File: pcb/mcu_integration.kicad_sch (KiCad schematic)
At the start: 36 parts, among them J5 DM3BT-DSF-PEJS, M1 MountingHole_Pad, M2 MountingHole_Pad, M3 MountingHole_Pad, M4 MountingHole_Pad, U1 STM32F103RBTx, U6 LM35DM, Y1 ECS-80-18-5PX-GM-TR

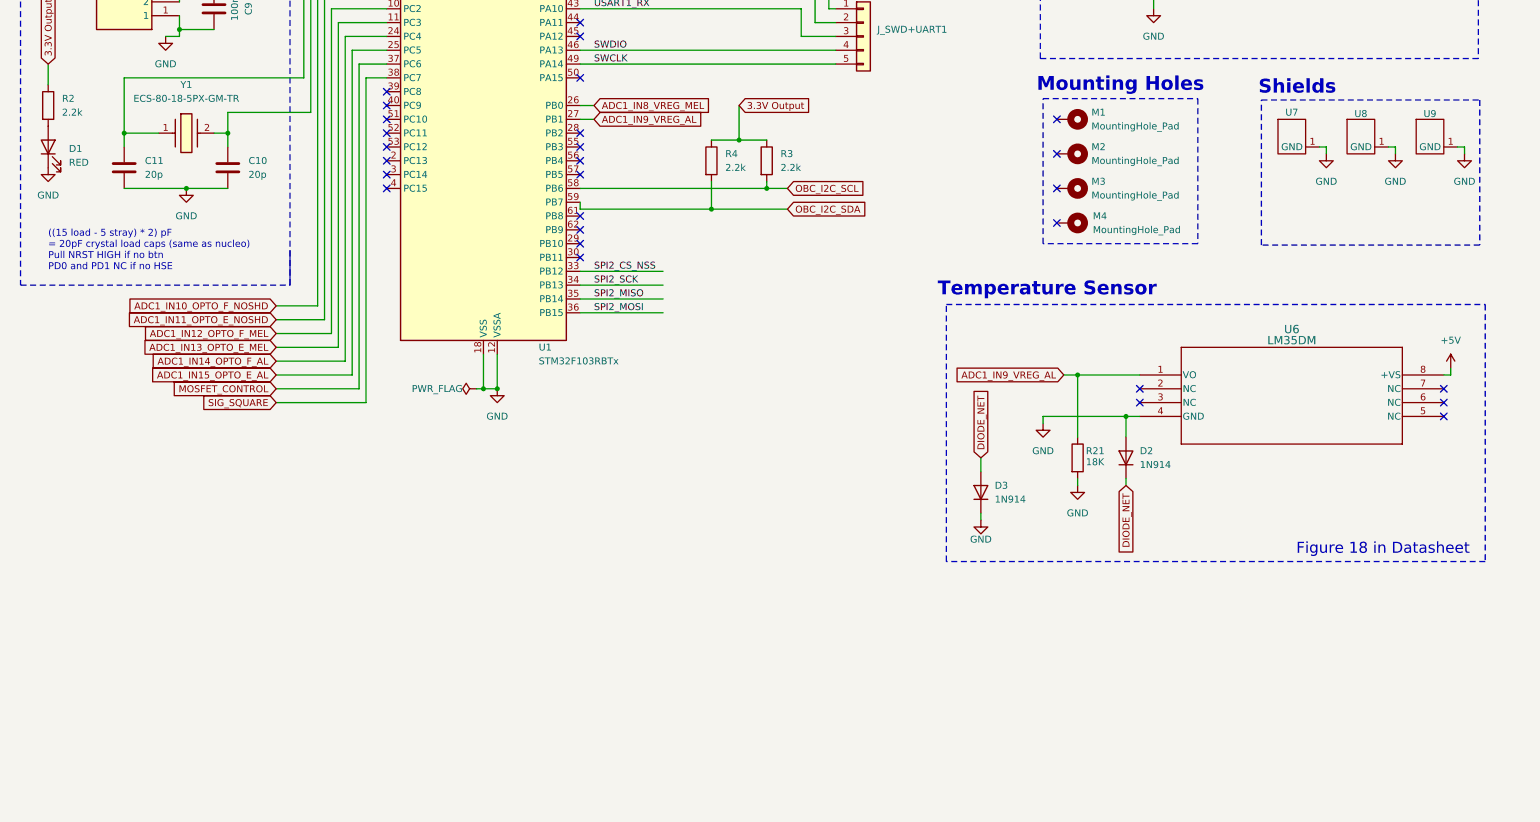
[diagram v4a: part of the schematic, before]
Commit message: Fixed Shield Solder Mask
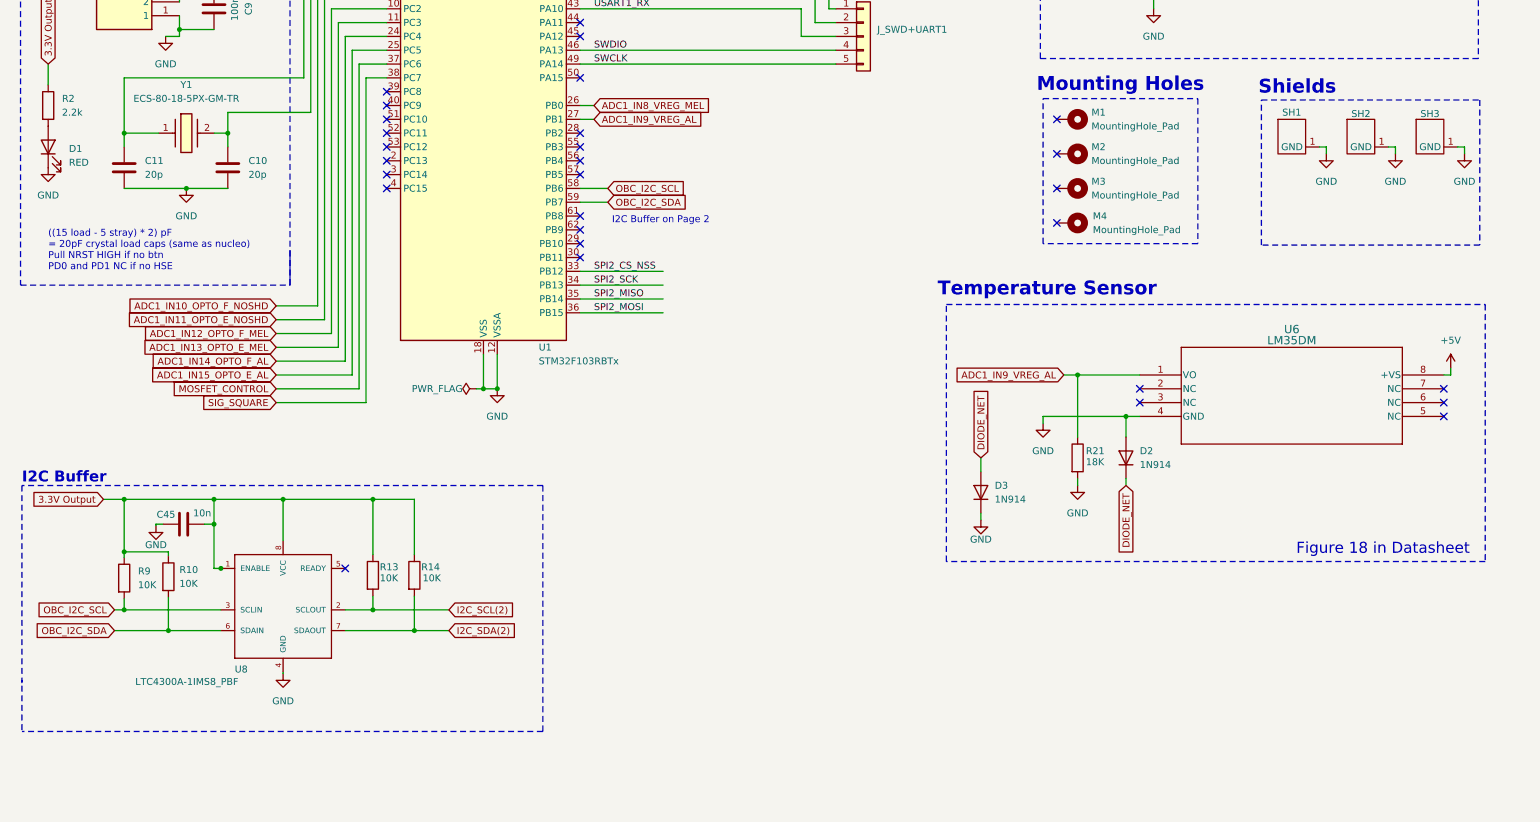
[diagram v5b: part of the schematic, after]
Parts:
- removed R3, R4: 2.2k, Resistor_SMD:R_0402_1005Metric, symbol Device:R
- added C45: 10n, Capacitor_SMD:C_0402_1005Metric, symbol Device:C
- added R10, R13, R14, R9: 10K, Resistor_SMD:R_0402_1005Metric, symbol Device:R
- added U8: LTC4300A-1IMS8_PBF, capstone:LTC4300A-1IMS8_PBF, symbol capstone:LTC4300A-1IMS8_PBF
- renumbered U7 to SH1, U8 to SH2, U9 to SH3
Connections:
- net 3.3V Output: now also C45.2, R10.1, R13.1, R14.1, R9.1, U8.1 (ENABLE), U8.8 (VCC)
- net GND: now also C45.1, U8.4 (GND)
- net OBC_I2C_SCL: now also R9.2, U8.3 (SCLIN)
- net OBC_I2C_SDA: now also R10.2, U8.6 (SDAIN)
- new net I2C_SCL(2): R13.2, U8.2 (SCLOUT)
- new net I2C_SDA(2): R14.2, U8.7 (SDAOUT)
- no-connect marks 34 -> 35
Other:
- note added: "I2C Buffer"
- note added: "I2C Buffer on Page 2"

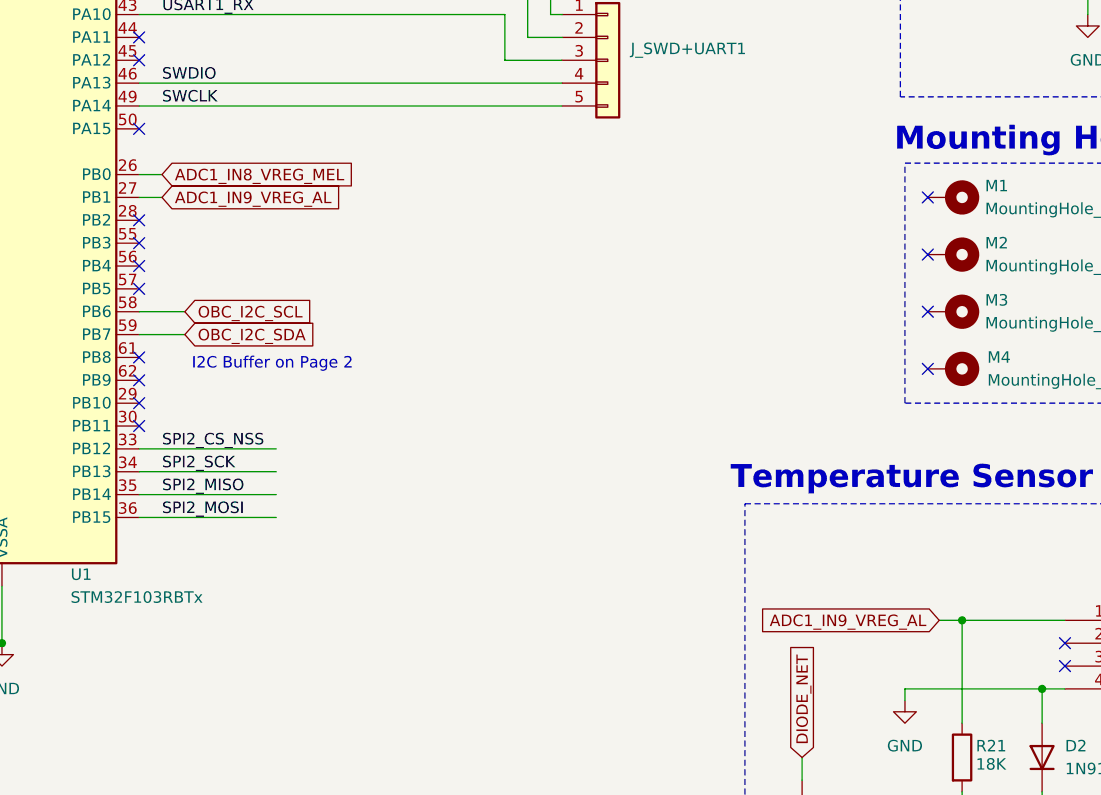
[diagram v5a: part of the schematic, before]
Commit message: Added switchable inputs for opamps
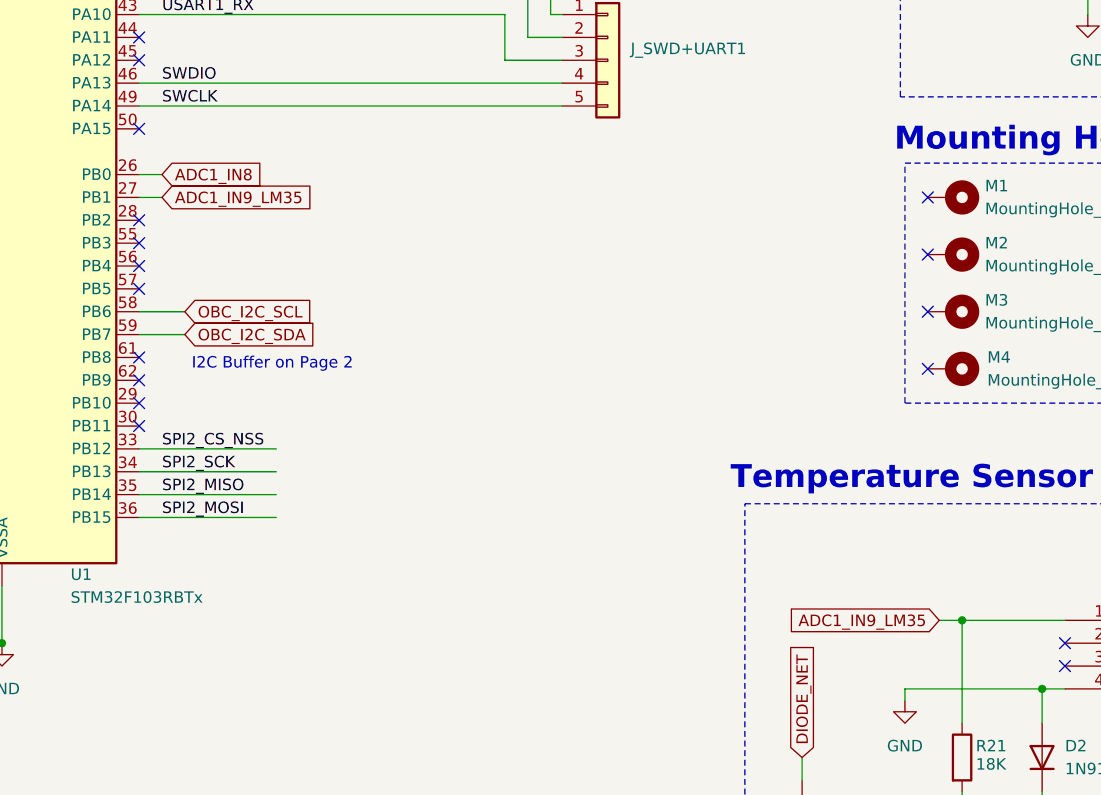
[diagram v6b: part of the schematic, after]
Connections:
- net ADC1_IN8_VREG_MEL renamed ADC1_IN8
- net ADC1_IN9_VREG_AL renamed ADC1_IN9_LM35
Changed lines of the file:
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@@
 		)
 	)
-	(global_label "ADC1_IN9_VREG_AL"
+	(global_label "ADC1_IN9_LM35"
 		(shape input)
 		(at 119.38 82.55 0)
@@
 		)
 		(property "Intersheetrefs" "${INTERSHEET_REFS}"
-			(at 140.1452 82.55 0)
+			(at 137.1818 82.55 0)
 			(effects
 				(font
@@
 		)
 	)
-	(global_label "ADC1_IN8_VREG_MEL"
+	(global_label "ADC1_IN8"
 		(shape input)
 		(at 119.38 80.01 0)
@@
 		)
 		(property "Intersheetrefs" "${INTERSHEET_REFS}"
-			(at 141.657 80.01 0)
+			(at 131.3157 80.01 0)
 			(effects
 				(font
@@
 		)
 	)
+	(global_label "ADC1_IN9_LM35"
+		(shape input)
+		(at 205.74 129.54 180)
+		(fields_autoplaced yes)
+		(effects
+			(font
+				(size 1.27 1.27)
+			)
+			(justify right)
+		)
+		(property "Intersheetrefs" "${INTERSHEET_REFS}"
+			(at 187.9382 129.54 0)
+			(effects
+				(font
+					(size 1.27 1.27)
+				)
+				(justify right)
+				(hide yes)
+			)
+		)
+	)
 	(global_label "ADC1_IN10_OPTO_F_NOSHD"
 		(shape input)
@@
 			(effects
 				(font
-					(size 1.27 1.27)
-				)
-				(justify right)
-				(hide yes)
-			)
-		)
-	)
-	(global_label "ADC1_IN9_VREG_AL"
-		(shape input)
-		(at 205.74 129.54 180)
-		(fields_autoplaced yes)
-		(effects
-			(font
-				(size 1.27 1.27)
-			)
-			(justify right)
-		)
-		(property "Intersheetrefs" "${INTERSHEET_REFS}"
-			(at 184.9748 129.54 0)
-			(effects
-				(font

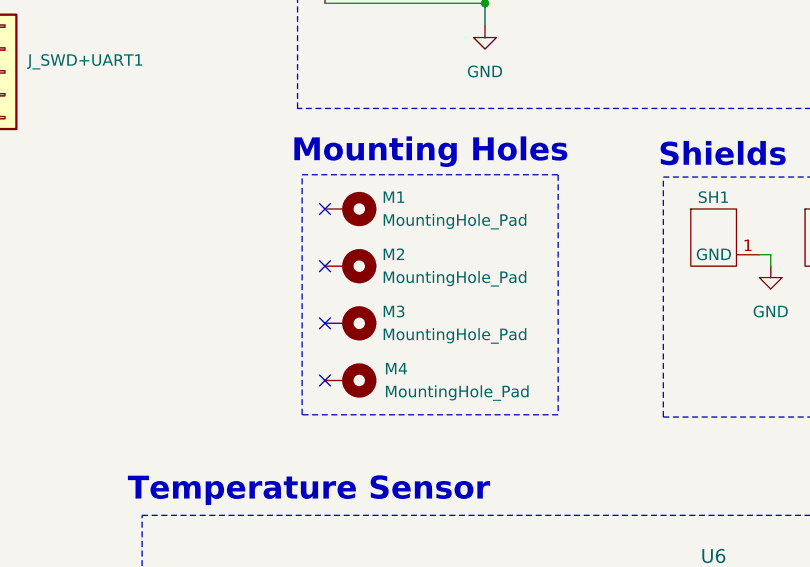
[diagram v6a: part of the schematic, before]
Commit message: Changed IC orientation
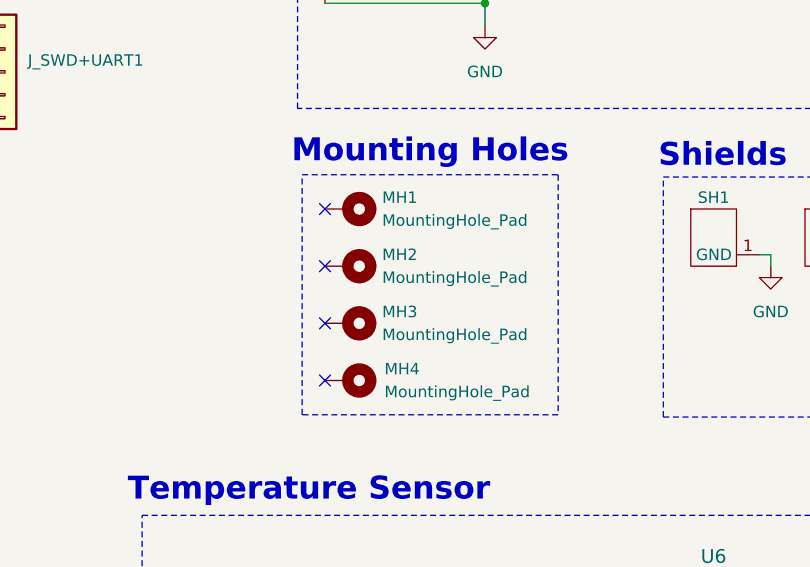
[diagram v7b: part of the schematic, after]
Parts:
- MH1: renamed from M1; footprint MountingHole:MountingHole_3.2mm_M3_Pad_Via -> capstone:MountingHole_3.18mm_6.35mm_Pad
- MH2: renamed from M2; footprint MountingHole:MountingHole_3.2mm_M3_Pad_Via -> capstone:MountingHole_3.18mm_6.35mm_Pad
- MH3: renamed from M3; footprint MountingHole:MountingHole_3.2mm_M3_Pad_Via -> capstone:MountingHole_3.18mm_6.35mm_Pad
- MH4: renamed from M4; footprint MountingHole:MountingHole_3.2mm_M3_Pad_Via -> capstone:MountingHole_3.18mm_6.35mm_Pad
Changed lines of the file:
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@@
 		(on_board yes)
 		(dnp no)
-		(property "Reference" "M4"
+		(property "Reference" "MH4"
 			(at 211.074 100.33 90)
 			(effects
@@
 			)
 		)
-		(property "Footprint" "MountingHole:MountingHole_3.2mm_M3_Pad_Via"
+		(property "Footprint" "capstone:MountingHole_3.18mm_6.35mm_Pad"
 			(at 207.01 101.6 0)
 			(effects
@@
 			(project "mcu_integration"
 				(path "/c0210bc3-f67f-47d8-a34e-f002a728adb2"
-					(reference "M4")
+					(reference "MH4")
 					(unit 1)
 				)
@@
 		(dnp no)
 		(fields_autoplaced yes)
-		(property "Reference" "M2"
+		(property "Reference" "MH2"
 			(at 210.82 87.6299 90)
 			(effects
@@
 			)
 		)
-		(property "Footprint" "MountingHole:MountingHole_3.2mm_M3_Pad_Via"
+		(property "Footprint" "capstone:MountingHole_3.18mm_6.35mm_Pad"
 			(at 207.01 88.9 0)
 			(effects
@@
 			(project "mcu_integration"
 				(path "/c0210bc3-f67f-47d8-a34e-f002a728adb2"
-					(reference "M2")
+					(reference "MH2")
 					(unit 1)
 				)
@@
 		(dnp no)
 		(fields_autoplaced yes)
-		(property "Reference" "M3"
+		(property "Reference" "MH3"
 			(at 210.82 93.9799 90)
 			(effects
@@
 			)
 		)
-		(property "Footprint" "MountingHole:MountingHole_3.2mm_M3_Pad_Via"
+		(property "Footprint" "capstone:MountingHole_3.18mm_6.35mm_Pad"
 			(at 207.01 95.25 0)
 			(effects
@@
 			(project "mcu_integration"
 				(path "/c0210bc3-f67f-47d8-a34e-f002a728adb2"
-					(reference "M3")
+					(reference "MH3")
 					(unit 1)
 				)
@@
 		(dnp no)
 		(fields_autoplaced yes)
-		(property "Reference" "M1"
+		(property "Reference" "MH1"
 			(at 210.82 81.2799 90)
 			(effects
@@
 			)
 		)
-		(property "Footprint" "MountingHole:MountingHole_3.2mm_M3_Pad_Via"
+		(property "Footprint" "capstone:MountingHole_3.18mm_6.35mm_Pad"
 			(at 207.01 82.55 0)
 			(effects
@@
 			(project "mcu_integration"
 				(path "/c0210bc3-f67f-47d8-a34e-f002a728adb2"
-					(reference "M1")
+					(reference "MH1")
 					(unit 1)
 				)

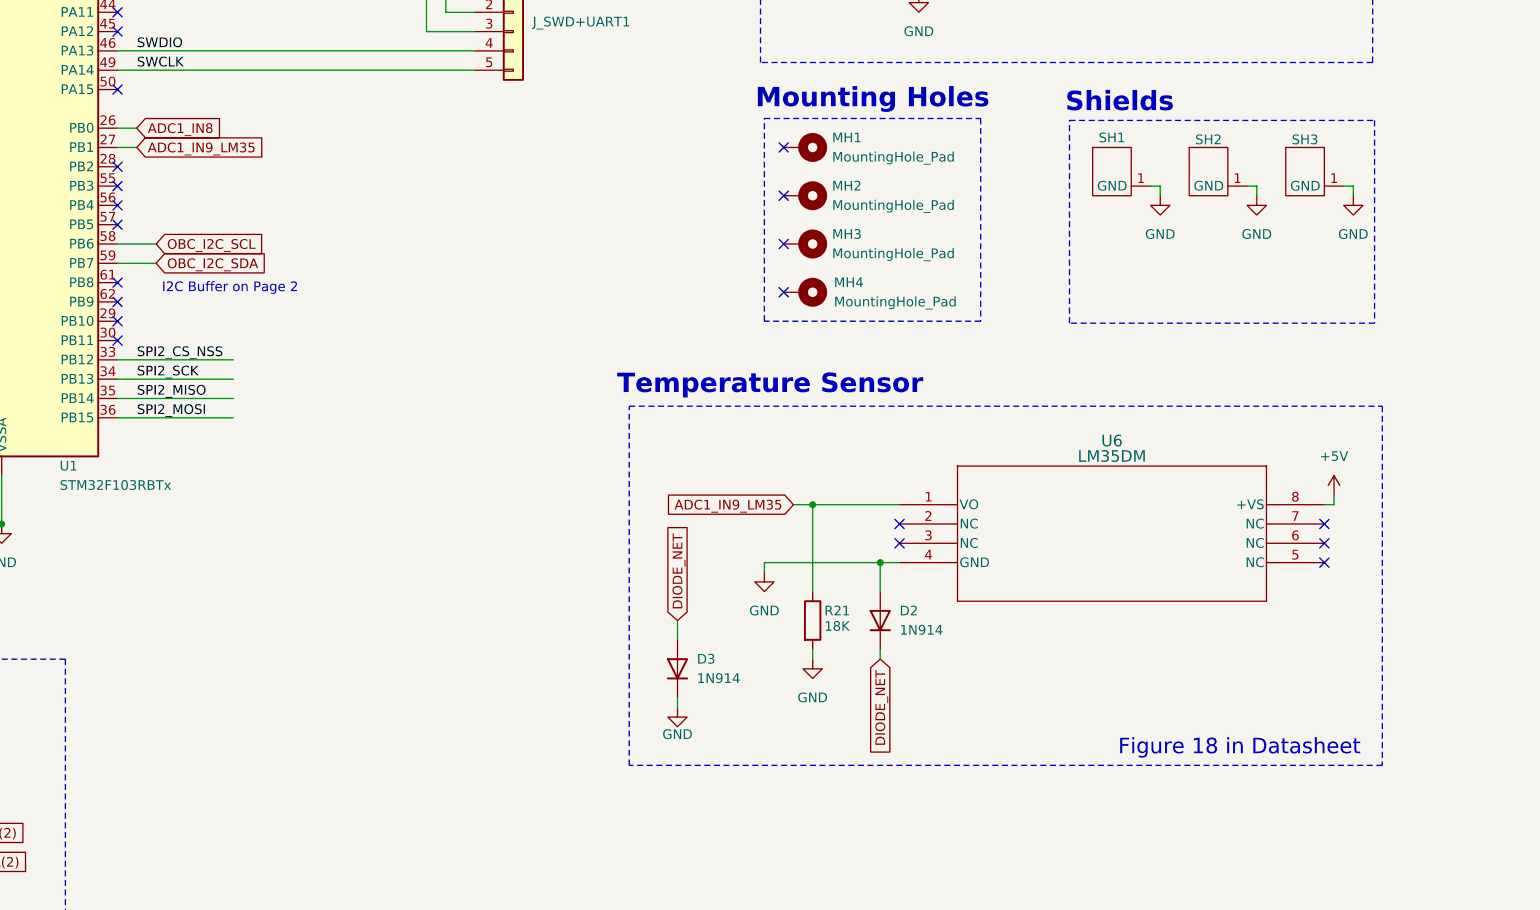
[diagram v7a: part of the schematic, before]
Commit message: Replaced LM35 temperature sensor with LMT87
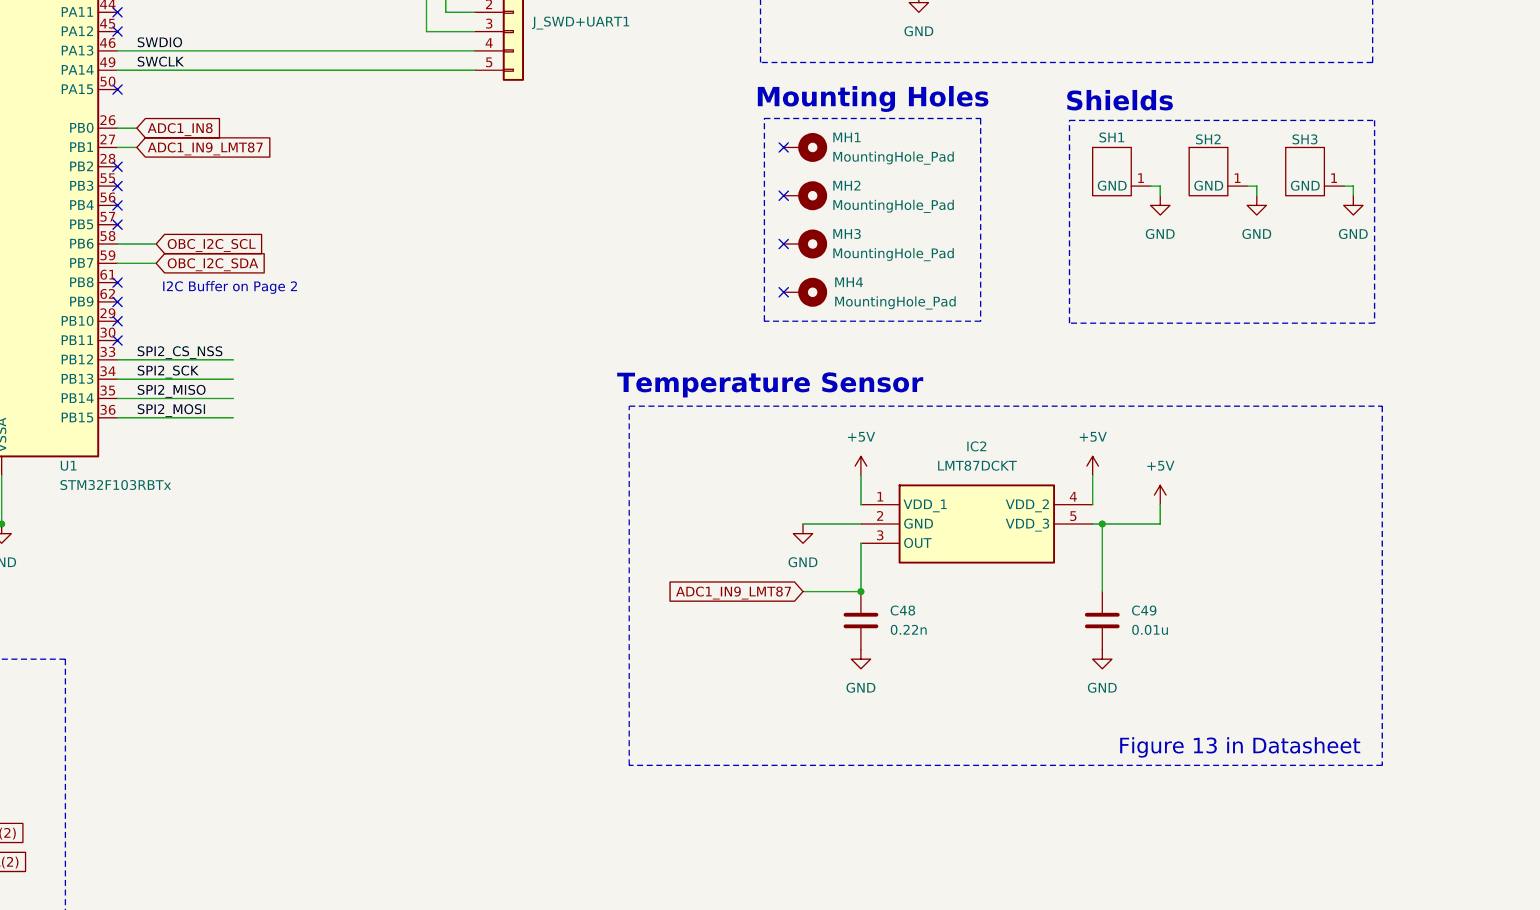
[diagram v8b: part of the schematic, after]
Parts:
- removed D2, D3: 1N914, capstone:SOD-323_1P7X1P25_ONS, symbol Device:D
- removed R21: 18K, Resistor_SMD:R_0402_1005Metric, symbol Device:R
- removed U6: LM35DM, capstone:LM35DM, symbol capstone:LM35DM
- added C48: 0.22n, Capacitor_SMD:C_0402_1005Metric, symbol Device:C
- added C49: 0.01u, Capacitor_SMD:C_0402_1005Metric, symbol Device:C
- added IC2: LMT87DCKT, SamacSys_Parts:SOT65P210X110-5N, symbol SamacSys_Parts:LMT87DCKT
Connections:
- net +5V: now also C49.1, IC2.1 (VDD_1), IC2.4 (VDD_2), IC2.5 (VDD_3)
- net GND: now also C48.2, C49.2, IC2.2 (GND)
- net ADC1_IN9_LM35 renamed ADC1_IN9_LMT87
- net ADC1_IN9_LMT87: now also C48.1, IC2.3 (OUT)
- no-connect marks 35 -> 30
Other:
- note added: "Figure 13 in Datasheet"
- note removed: "Figure 18 in Datasheet"
